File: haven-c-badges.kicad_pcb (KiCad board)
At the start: 2 copper layers, 58.4 x 36.8 mm, 7 parts, among them U1 NT3H2111W0FHKH

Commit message: he was whipping up straight poison in a kettle
- WHY CANT I GET THESE TWO PADS TO CONNECT IDK ABOUT THE POLARITY pls help
- i switched all the footprints and symbols around like 3 times
- the antennas are wired up correctly now I think 💔(manual net assigning at the antenna pads)
a. polarity is not in antennas
b. but the nets not connected by default is rlly bugging me
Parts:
- L1: footprint EasyEDA2Kicad:25X48MM_NFC_ANTENNA manualimport -> NFC Components:25X48MM_NFC_ANTENNA
- U1: footprint EasyEDA2Kicad:XQFN-8_L1.6-W1.6-P0.50-BL_NT3H2111W0FHKH -> NFC Components:XQFN-8_L1.6-W1.6-P0.50-BL_NT3H2111W0FHKH
- moved L1 97.1 mm to (151.9, 95.6)
- moved U1 84.5 mm to (149.8, 65.6)
- moved U1 78.3 mm to (148.6, 78.9), turned to -90 degrees
- moved D1 64.9 mm to (136.2, 78.3), turned to 90 degrees
- moved R1 60.4 mm to (146.4, 78.7)
- moved C1 56.3 mm to (148.0, 76.2), turned to 180 degrees
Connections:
- L1 pad P$1: (no net) -> Net-(U1-LB)
- L1 pad P$2: (no net) -> Net-(U1-LA)
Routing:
- net Net-(D1-K): track 0.00 -> 15.7 mm
- net Net-(D1-A): track 0.00 -> 10.8 mm
- net Net-(U1-LA): track 0.00 -> 9.85 mm, vias 0 -> 1
- net Net-(U1-VCC): track 0.00 -> 6.98 mm
- net Net-(U1-LB): track 0.00 -> 3.71 mm
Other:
- outline, holes or cut-outs redrawn

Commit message: idk bro I did the other things incl silkscreen a bit + journal?
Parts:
- added G***: LOGO, LOGO, F.Cu at (126.1, 92.5)
- moved G*** 7.17 mm to (154.3, 103.3)
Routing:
- net Net-(U1-LA): track 9.85 -> 11.6 mm
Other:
- board size 58.4 x 36.8 mm -> 103.3 x 78.6 mm
- board text added: "Designed by Henry W SM"
- board text added: "PCBs provided by"

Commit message: idk some scaling adjustment things
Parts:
- added C1: 220nF, EasyEDA2Kicad:C0603, F.Cu at (199.6, 128.5)
- added D1: LED, EasyEDA2Kicad:LED0805-R-RD, F.Cu at (201.7, 140.3)
- added G***: LOGO, LOGO, F.Cu at (118.0, 119.1)
- added G***: LOGO, LOGO, F.Cu at (53.5, 78.5)
- added L1: 25X48MM_NFC_ANTENNA, NFC Components:25X48MM_NFC_ANTENNA, F.Cu at (219.0, 124.6)
- added R1: 47*, EasyEDA2Kicad:R0603, F.Cu at (202.1, 130.1)
- added REF**: MountingHole_4.3x6.2mm_M4_Pad, MountingHole:MountingHole_4.3x6.2mm_M4_Pad, F.Cu at (84.0, 113.5)
- added U1: NT3H2111W0FHKH, NFC Components:XQFN-8_L1.6-W1.6-P0.50-BL_NT3H2111W0FHKH, F.Cu at (202.3, 127.9)
- moved C1 45.7 mm to (148.0, 30.5)
- moved G*** 45.7 mm to (154.3, 57.6)
- moved G*** 45.7 mm to (126.1, 46.8)
- moved L1 45.7 mm to (151.9, 49.9)
- moved R1 45.7 mm to (146.4, 33.0)
- moved U1 45.7 mm to (148.6, 33.2)
- moved D1 45.7 mm to (136.2, 32.6)
- moved U1 16.3 mm to (148.1, 49.4)
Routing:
- net Net-(D1-K): track 15.7 -> 31.4 mm
- net Net-(U1-LA): track 11.6 -> 23.2 mm, vias 1 -> 2
- net Net-(D1-A): track 10.8 -> 21.6 mm
- net Net-(U1-VCC): track 6.98 -> 14.0 mm
- net Net-(U1-LB): track 3.71 -> 7.42 mm
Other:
- board size 103.3 x 78.6 mm -> 104.5 x 109.7 mm

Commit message: cleared everything out except real looking thing + more readme
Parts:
- removed the C1 at (199.6, 128.5)
- removed the D1 at (201.7, 140.3)
- removed G*** (x4): LOGO, LOGO
- removed the L1 at (219.0, 124.6)
- removed the R1 at (202.1, 130.1)
- removed the REF** at (84.0, 113.5)
- removed the U1 at (148.1, 49.4)
- removed the U1 at (202.3, 127.9)
- added Bottom Silkscreen: LOGO, LOGO, B.Cu at (251.6, 85.5)
- added REF**: Lanyard_hole2, Lanyard_hole2, F.Cu at (251.3, 42.5)
- added REF**: Lanyard_hole2, Lanyard_hole2, F.Cu at (134.3, 50.2)
- added UV Print Guide: LOGO, LOGO, F.Cu at (251.6, 85.5)
- moved D1 152.4 mm to (251.6, 132.1), turned to 180 degrees
- moved R1 134.9 mm to (250.6, 118.6), turned to 90 degrees
- moved C1 134.3 mm to (248.6, 119.4), turned to 0 degrees
- moved U1 131.1 mm to (248.8, 117.8), turned to 0 degrees
- moved L1 109.7 mm to (248.6, 101.7), turned to 180 degrees
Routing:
- net Net-(U1-LA): track 23.2 -> 6.56 mm, vias 2 -> 1
- net Net-(D1-K): track 31.4 -> 16.0 mm
- net Net-(U1-VCC): track 14.0 -> 3.84 mm
- net Net-(D1-A): track 21.6 -> 13.6 mm
- net Net-(U1-LB): track 7.42 -> 1.76 mm
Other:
- board size 104.5 x 109.7 mm -> 173.3 x 99.2 mm
- board text added: "0.125"
- board text removed: "PCBs provided by"

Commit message: I made some stuff with the gerbers
- Copper outlines
- Things
- Background art
- Exported v1 but its already outdated from the figma i used
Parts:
- removed Bottom Silkscreen: LOGO, LOGO
- added BottomSilkscreen: LOGO, LOGO, B.Cu at (181.4, 97.2)
- moved REF** 71.1 mm to (64.2, 61.9)
- moved C1 71.1 mm to (178.5, 131.1)
- moved D1 71.1 mm to (181.5, 143.8)
- moved L1 71.1 mm to (178.5, 113.4)
- moved R1 71.1 mm to (180.5, 130.3)
- moved REF** 71.1 mm to (181.2, 54.1)
- moved U1 71.1 mm to (178.6, 129.6)
- moved UV Print Guide 71.1 mm to (181.4, 97.2)
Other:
- board text removed: "Designed by Henry W SM"

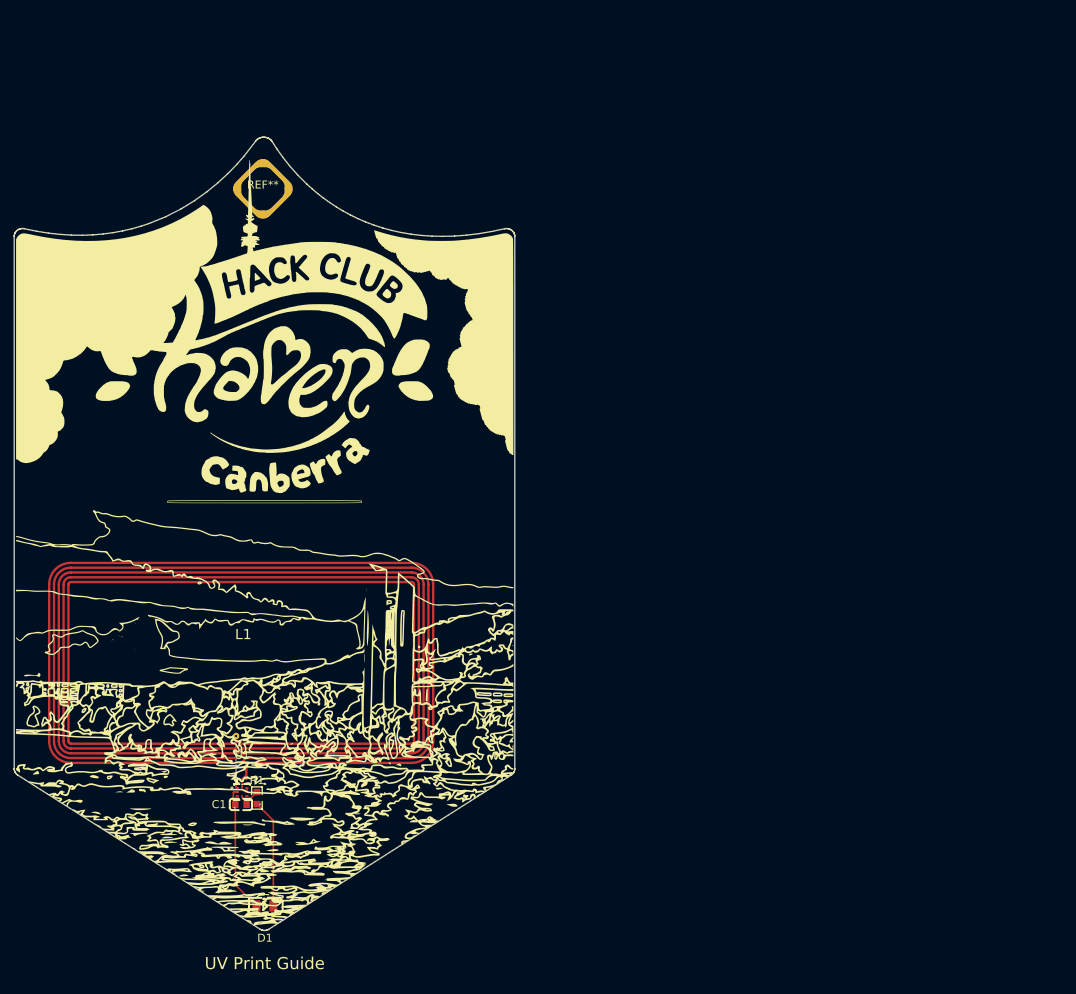
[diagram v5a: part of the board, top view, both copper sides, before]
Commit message: imported most of the updated graphics
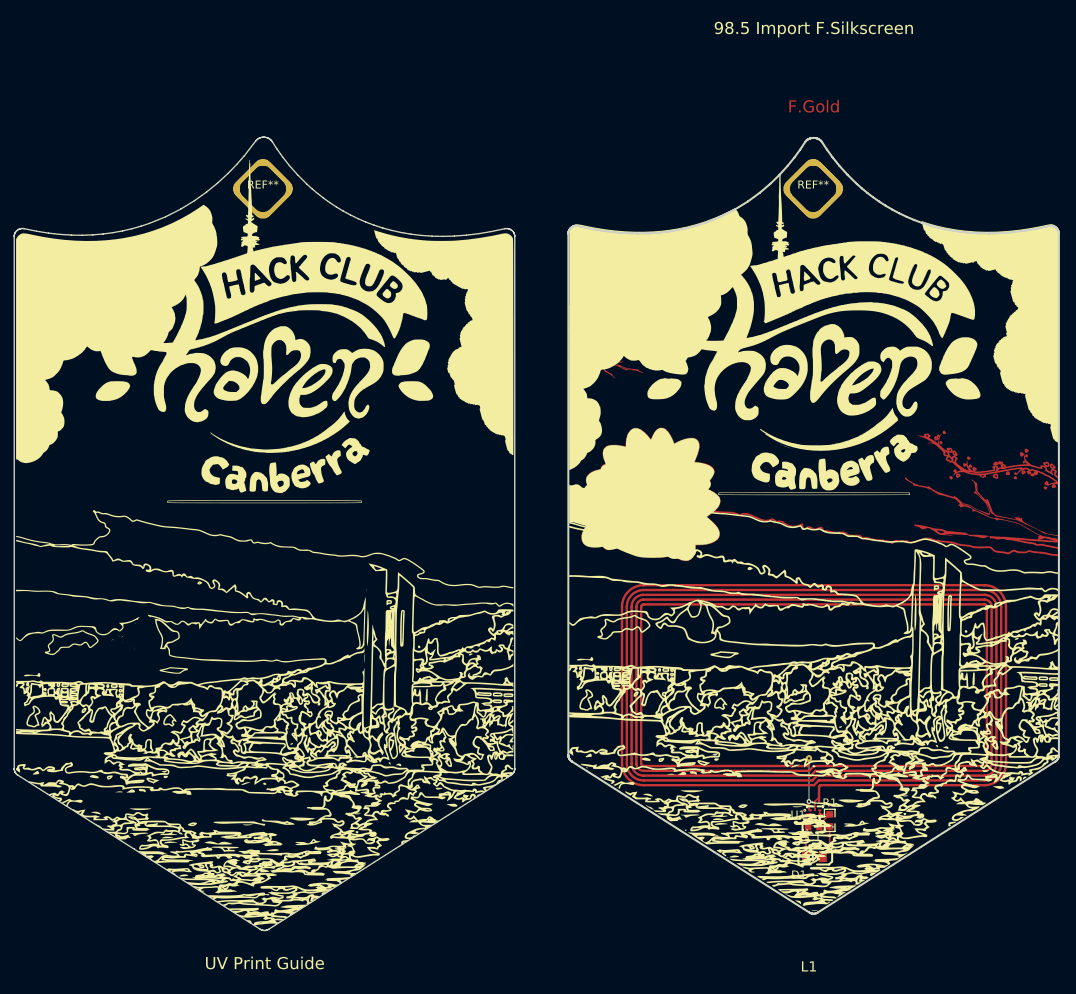
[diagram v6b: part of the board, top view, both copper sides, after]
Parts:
- added 98.5 Import F.Silkscreen: LOGO, LOGO, F.Cu at (250.1, 95.5)
- added B.Silkscreen: LOGO, LOGO, B.Cu at (250.1, 95.3)
- added F.Gold, F.Mask: LOGO, LOGO, F.Cu at (250.1, 95.5)
- added F.Soldermask: LOGO, LOGO, F.Cu at (319.6, 95.5)
- added REF**: Lanyard_hole2, Lanyard_hole2, F.Cu at (250.0, 54.1)
- moved C1 71.7 mm to (250.1, 133.9)
- moved L1 71.7 mm to (250.1, 116.2)
- moved R1 71.7 mm to (252.1, 133.1)
- moved U1 71.7 mm to (250.2, 132.3)
- moved D1 69.0 mm to (250.2, 137.6)
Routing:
- net Net-(D1-K): track 16.0 -> 6.00 mm
- net Net-(D1-A): track 13.6 -> 4.11 mm
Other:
- board size 173.3 x 99.2 mm -> 241.3 x 99.2 mm
